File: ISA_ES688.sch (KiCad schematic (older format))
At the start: 108 parts, among them J1 ISA BUS, J2 Interrupt Select, J3 Address Select, J4 DMA Select, J5 Joystick/MIDI, J6 LINE OUT, J7 MIC, J8 LINE IN, J9 SPKR OUT, U1 74LS14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

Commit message: Finished assigning footprints
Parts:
- U3: footprint (none) -> Package_DIP:DIP-16_W7.62mm
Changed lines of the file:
@@
 F 0 "U3" H 8150 15050 60  0000 C CNN
 F 1 "NE558" H 8600 15050 60  0000 C CNN
-F 2 "" H 8900 14500 60  0001 C CNN
+F 2 "Package_DIP:DIP-16_W7.62mm" H 8900 14500 60  0001 C CNN
 F 3 "" H 8900 14500 60  0000 C CNN
 	1    8400 14300

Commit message: Begin laying out parts
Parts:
- removed C3: 100nF, Capacitor_SMD:C_1206_3216Metric_Pad1.33x1.80mm_HandSolder, symbol Device:C_Small
- C10, C13, C14, C15, C16, C17, C18, C19, C25, C5, C6, C7: footprint Capacitor_SMD:C_1206_3216Metric_Pad1.33x1.80mm_HandSolder -> Capacitor_THT:C_Disc_D5.0mm_W2.5mm_P5.00mm
- U2, U4: footprint Package_SO:SOIC-20W_7.5x12.8mm_P1.27mm -> Package_DIP:DIP-20_W7.62mm
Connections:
- net D0: now also U4.2 (A0); no longer U4.9 (A7)
- net D1: now also U4.3 (A1); no longer U4.8 (A6)
- net D2: now also U4.4 (A2); no longer U4.7 (A5)
- net D3: now also U4.5 (A3); no longer U4.6 (A4)
- net D4: now also U4.6 (A4); no longer U4.5 (A3)
- net D5: now also U4.7 (A5); no longer U4.4 (A2)
- net D6: now also U4.8 (A6); no longer U4.3 (A1)
- net D7: now also U4.9 (A7); no longer U4.2 (A0)
- net ES-D0: now also U4.18 (B0); no longer U4.11 (B7)
- net ES-D1: now also U4.17 (B1); no longer U4.12 (B6)
- net ES-D2: now also U4.16 (B2); no longer U4.13 (B5)
- net ES-D3: now also U4.15 (B3); no longer U4.14 (B4)
- net ES-D4: now also U4.14 (B4); no longer U4.15 (B3)
- net ES-D5: now also U4.13 (B5); no longer U4.16 (B2)
- net ES-D6: now also U4.12 (B6); no longer U4.17 (B1)
- net ES-D7: now also U4.11 (B7); no longer U4.18 (B0)
- net GNDA: now also RV1.4; no longer RV1.6
- net at C39.2: now also RV1.6; no longer RV1.4
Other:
- moved on the sheet: U4

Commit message: Begin placing some components on the board
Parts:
- C11, C12: footprint Capacitor_THT:C_Disc_D3.8mm_W2.6mm_P2.50mm -> Capacitor_SMD:C_1206_3216Metric_Pad1.33x1.80mm_HandSolder
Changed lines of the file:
@@
 F 0 "C12" V 10500 7350 50  0000 L CNN
 F 1 "10pF" V 10500 7150 50  0000 L CNN
-F 2 "Capacitor_THT:C_Disc_D3.8mm_W2.6mm_P2.50mm" H 10600 7200 50  0001 C CNN
+F 2 "Capacitor_SMD:C_1206_3216Metric_Pad1.33x1.80mm_HandSolder" H 10600 7200 50  0001 C CNN
 F 3 "~" H 10600 7200 50  0001 C CNN
 	1    10600 7200
@@
 F 0 "C11" V 10500 7150 50  0000 L CNN
 F 1 "10pF" V 10500 6950 50  0000 L CNN
-F 2 "Capacitor_THT:C_Disc_D3.8mm_W2.6mm_P2.50mm" H 10600 7000 50  0001 C CNN
+F 2 "Capacitor_SMD:C_1206_3216Metric_Pad1.33x1.80mm_HandSolder" H 10600 7000 50  0001 C CNN
 F 3 "~" H 10600 7000 50  0001 C CNN
 	1    10600 7000

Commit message: More movement on PCB
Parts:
- J7: footprint Connector_PinHeader_2.54mm:PinHeader_1x02_P2.54mm_Horizontal -> Connector_PinHeader_2.54mm:PinHeader_1x02_P2.54mm_Vertical
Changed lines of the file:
@@
 F 0 "J7" H 15622 3182 50  0000 R CNN
 F 1 "MIC" H 15622 3273 50  0000 R CNN
-F 2 "Connector_PinHeader_2.54mm:PinHeader_1x02_P2.54mm_Horizontal" H 15650 3300 50  0001 C CNN
+F 2 "Connector_PinHeader_2.54mm:PinHeader_1x02_P2.54mm_Vertical" H 15650 3300 50  0001 C CNN
 F 3 "~" H 15650 3300 50  0001 C CNN
 	1    15650 3300

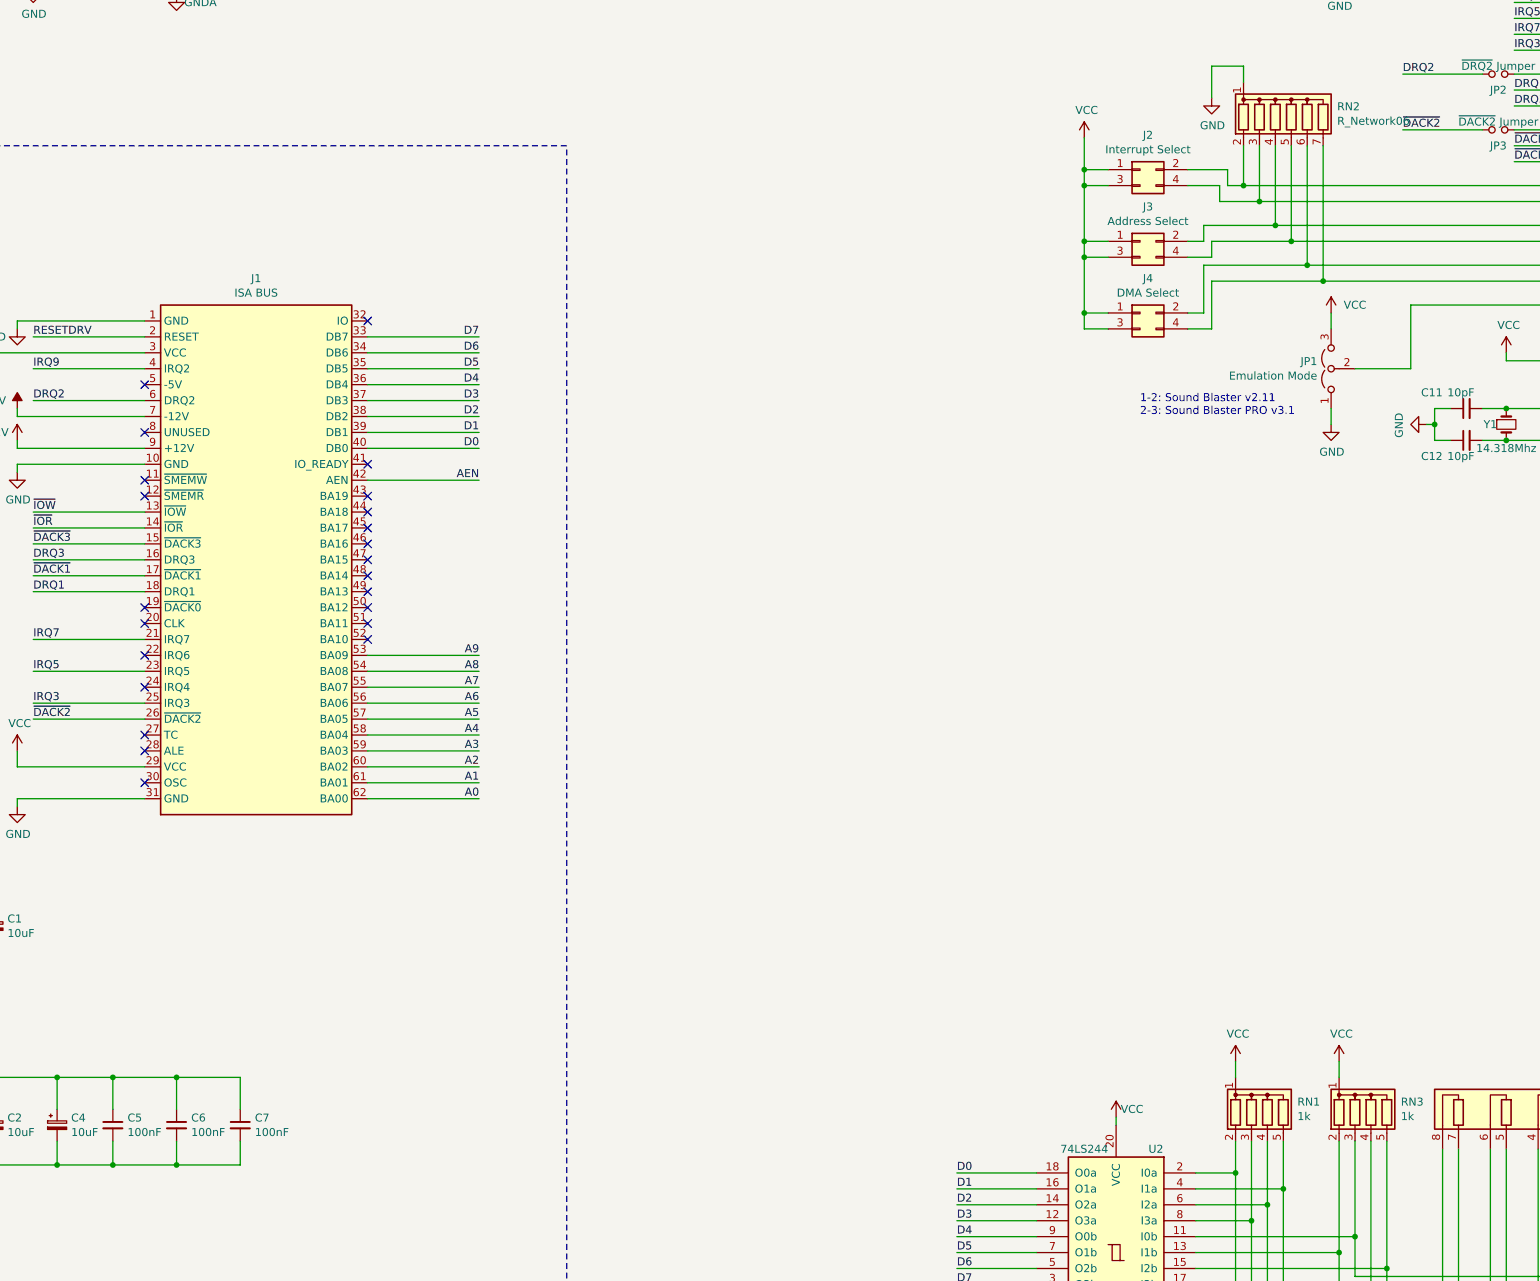
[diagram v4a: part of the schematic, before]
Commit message: Additional trace routing
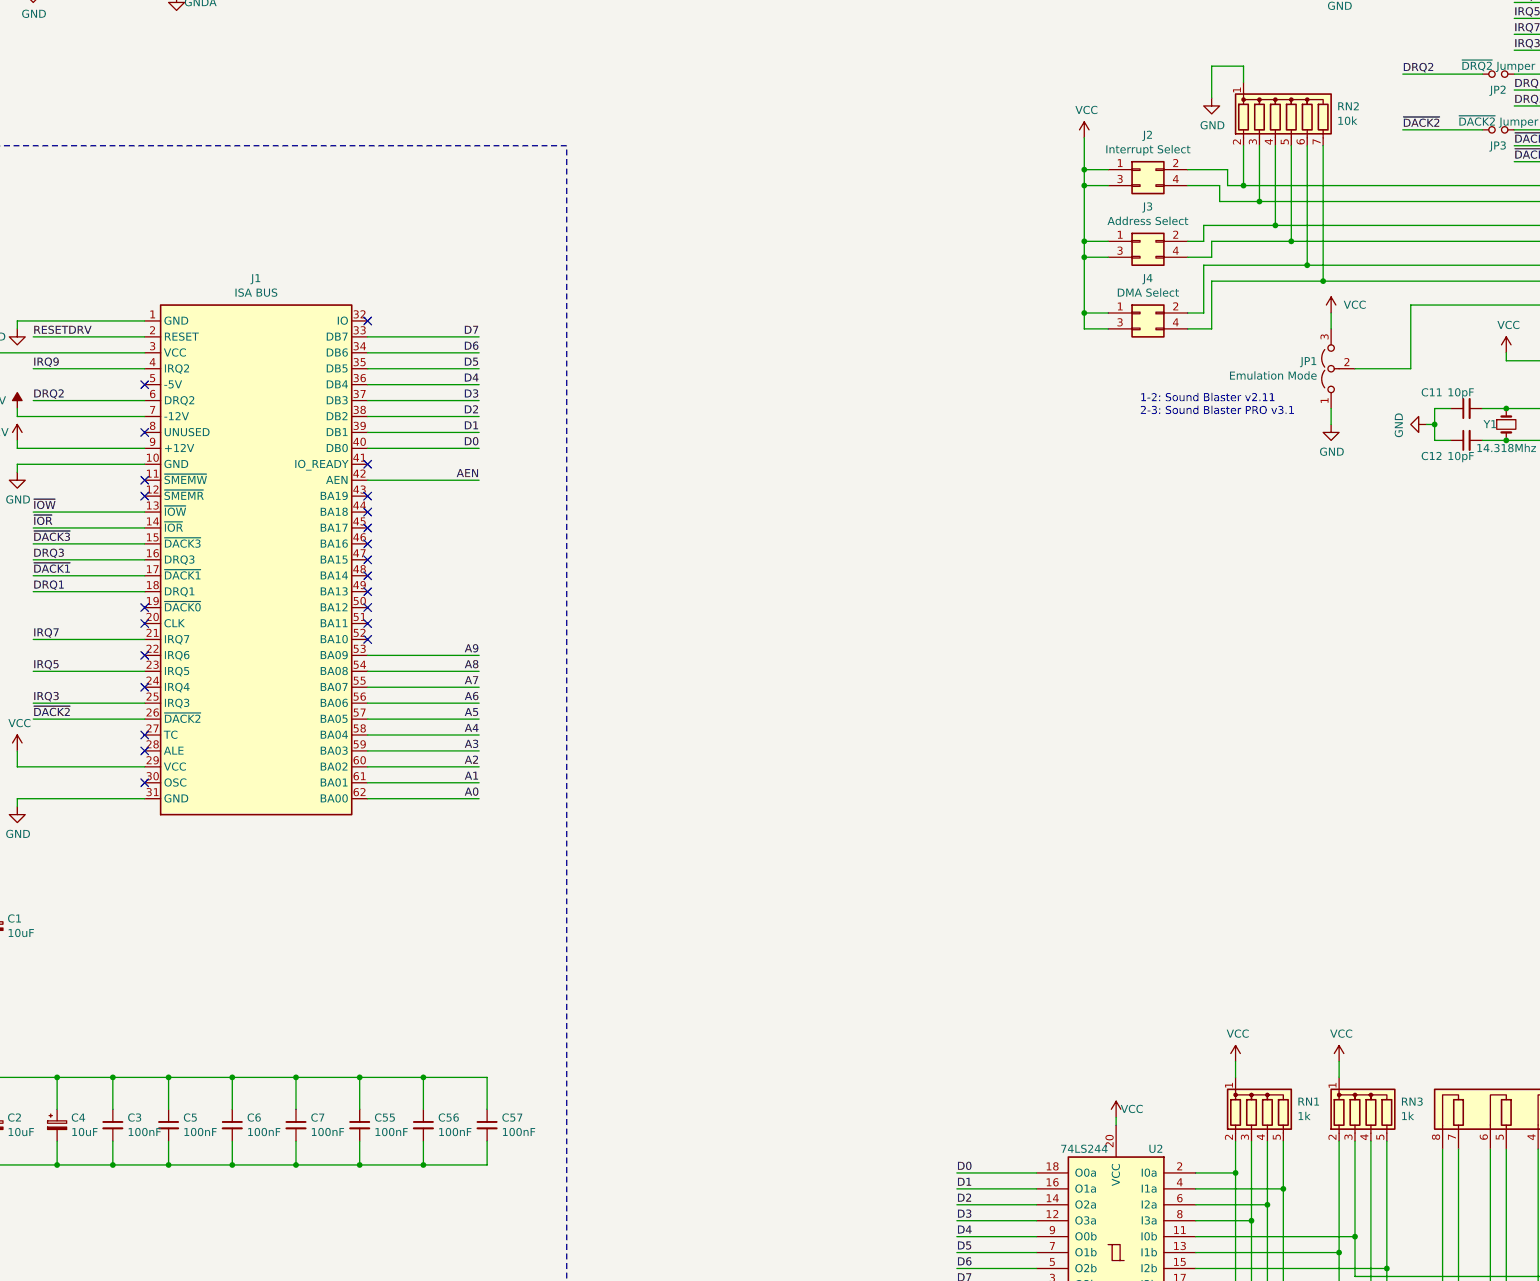
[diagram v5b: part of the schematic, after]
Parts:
- added C3, C55, C56, C57: 100nF, Capacitor_SMD:C_1206_3216Metric_Pad1.33x1.80mm_HandSolder, symbol Device:C_Small
- RN2: value R_Network06 -> 10k
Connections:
- net GND: now also C3.2, C55.2, C56.2, C57.2
- net VCC: now also C3.1, C55.1, C56.1, C57.1
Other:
- moved on the sheet: C5, C6, C7
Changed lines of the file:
@@
 $EndComp
 Wire Wire Line
-	2500 11750 2900 11750
-Connection ~ 2500 11750
-Wire Wire Line
-	2500 11600 2500 11750
-Connection ~ 2100 11750
-Wire Wire Line
-	2900 11750 2900 11600
-Wire Wire Line
-	2100 11750 2500 11750
-Wire Wire Line
-	2500 11200 2900 11200
-Connection ~ 2500 11200
-Wire Wire Line
-	2500 11400 2500 11200
-Connection ~ 2100 11200
-Wire Wire Line
-	2900 11200 2900 11400
-Wire Wire Line
-	2100 11200 2500 11200
+	2850 11750 3250 11750
+Connection ~ 2850 11750
+Wire Wire Line
+	2850 11600 2850 11750
+Connection ~ 2450 11750
+Wire Wire Line
+	3250 11750 3250 11600
+Wire Wire Line
+	2450 11750 2850 11750
+Wire Wire Line
+	2850 11200 3250 11200
+Connection ~ 2850 11200
+Wire Wire Line
+	2850 11400 2850 11200
+Connection ~ 2450 11200
+Wire Wire Line
+	3250 11200 3250 11400
+Wire Wire Line
+	2450 11200 2850 11200
 $Comp
 L Device:C_Small C7
 U 1 1 609B89C1
-P 2900 11500
-F 0 "C7" H 2992 11546 50  0000 L CNN
-F 1 "100nF" H 2992 11455 50  0000 L CNN
-F 2 "Capacitor_THT:C_Disc_D5.0mm_W2.5mm_P5.00mm" H 2900 11500 50  0001 C CNN
-F 3 "~" H 2900 11500 50  0001 C CNN
-	1    2900 11500
+P 3250 11500
+F 0 "C7" H 3342 11546 50  0000 L CNN
+F 1 "100nF" H 3342 11455 50  0000 L CNN
+F 2 "Capacitor_THT:C_Disc_D5.0mm_W2.5mm_P5.00mm" H 3250 11500 50  0001 C CNN
+F 3 "~" H 3250 11500 50  0001 C CNN
+	1    3250 11500
 	1    0    0    -1
 $EndComp
@@
 L Device:C_Small C6
 U 1 1 609B7B2F
-P 2500 11500
-F 0 "C6" H 2592 11546 50  0000 L CNN
-F 1 "100nF" H 2592 11455 50  0000 L CNN
-F 2 "Capacitor_THT:C_Disc_D5.0mm_W2.5mm_P5.00mm" H 2500 11500 50  0001 C CNN
-F 3 "~" H 2500 11500 50  0001 C CNN
-	1    2500 11500
+P 2850 11500
+F 0 "C6" H 2942 11546 50  0000 L CNN
+F 1 "100nF" H 2942 11455 50  0000 L CNN
+F 2 "Capacitor_THT:C_Disc_D5.0mm_W2.5mm_P5.00mm" H 2850 11500 50  0001 C CNN
+F 3 "~" H 2850 11500 50  0001 C CNN
+	1    2850 11500
 	1    0    0    -1
 $EndComp
@@
 NoConn ~ 2300 9050
 Wire Wire Line
-	2100 11600 2100 11750
-Wire Wire Line
-	2100 11400 2100 11200
-Connection ~ 1750 11750
-Wire Wire Line
-	1750 11750 2100 11750
-Connection ~ 1750 11200
-Wire Wire Line
-	1750 11200 2100 11200
+	2450 11600 2450 11750
+Wire Wire Line
+	2450 11400 2450 11200
+Wire Wire Line
+	2100 11750 2450 11750
+Wire Wire Line
+	2100 11200 2450 11200
 $Comp
 L power:VCC #PWR05
@@
 L Device:C_Small C5
 U 1 1 612431D5
-P 2100 11500
-F 0 "C5" H 2192 11546 50  0000 L CNN
-F 1 "100nF" H 2192 11455 50  0000 L CNN
-F 2 "Capacitor_THT:C_Disc_D5.0mm_W2.5mm_P5.00mm" H 2100 11500 50  0001 C CNN
-F 3 "~" H 2100 11500 50  0001 C CNN
-	1    2100 11500
+P 2450 11500
+F 0 "C5" H 2542 11546 50  0000 L CNN
+F 1 "100nF" H 2542 11455 50  0000 L CNN
+F 2 "Capacitor_THT:C_Disc_D5.0mm_W2.5mm_P5.00mm" H 2450 11500 50  0001 C CNN
+F 3 "~" H 2450 11500 50  0001 C CNN
+	1    2450 11500
 	1    0    0    -1
 $EndComp
@@
 P 9500 5150
 F 0 "RN2" H 9788 5196 50  0000 L CNN
-F 1 "R_Network06" H 9788 5105 50  0000 L CNN
+F 1 "10k" H 9788 5105 50  0000 L CNN
 F 2 "Resistor_THT:R_Array_SIP7" V 9875 5150 50  0001 C CNN
 F 3 "http://www.vishay.com/docs/31509/csc.pdf" H 9500 5150 50  0001 C CNN
@@
 Wire Wire Line
 	17300 4700 17300 4750
+Wire Wire Line
+	2100 11600 2100 11750
+Wire Wire Line
+	2100 11400 2100 11200
+Wire Wire Line
+	1750 11750 2100 11750
+Wire Wire Line
+	1750 11200 2100 11200
+$Comp
+L Device:C_Small C3
+U 1 1 61CFC5F5
+P 2100 11500
+F 0 "C3" H 2192 11546 50  0000 L CNN
+F 1 "100nF" H 2192 11455 50  0000 L CNN
+F 2 "Capacitor_SMD:C_1206_3216Metric_Pad1.33x1.80mm_HandSolder" H 2100 11500 50  0001 C CNN
+F 3 "~" H 2100 11500 50  0001 C CNN
+	1    2100 11500
+	1    0    0    -1
+$EndComp
+Connection ~ 1750 11200
+Connection ~ 1750 11750
+Connection ~ 2100 11200
+Connection ~ 2100 11750
+$Comp
+L Device:C_Small C55
+U 1 1 61F8828C
+P 3650 11500
+F 0 "C55" H 3742 11546 50  0000 L CNN
+F 1 "100nF" H 3742 11455 50  0000 L CNN
+F 2 "Capacitor_SMD:C_1206_3216Metric_Pad1.33x1.80mm_HandSolder" H 3650 11500 50  0001 C CNN
+F 3 "~" H 3650 11500 50  0001 C CNN
+	1    3650 11500
+	1    0    0    -1
+$EndComp
+$Comp
+L Device:C_Small C56
+U 1 1 61F8970B
+P 4050 11500
+F 0 "C56" H 4142 11546 50  0000 L CNN
+F 1 "100nF" H 4142 11455 50  0000 L CNN
+F 2 "Capacitor_SMD:C_1206_3216Metric_Pad1.33x1.80mm_HandSolder" H 4050 11500 50  0001 C CNN
+F 3 "~" H 4050 11500 50  0001 C CNN
+	1    4050 11500
+	1    0    0    -1
+$EndComp
+Wire Wire Line
+	3250 11200 3650 11200
+Wire Wire Line
+	4050 11200 4050 11400
+Connection ~ 3250 11200
+Wire Wire Line
+	3650 11400 3650 11200
+Connection ~ 3650 11200
+Wire Wire Line
+	3650 11200 4050 11200
+Wire Wire Line
+	3250 11750 3650 11750
+Wire Wire Line
+	4050 11750 4050 11600
+Connection ~ 3250 11750
+Wire Wire Line
+	3650 11600 3650 11750
+Connection ~ 3650 11750
+Wire Wire Line
+	3650 11750 4050 11750
+$Comp
+L Device:C_Small C57
+U 1 1 621D6566
+P 4450 11500
+F 0 "C57" H 4542 11546 50  0000 L CNN
+F 1 "100nF" H 4542 11455 50  0000 L CNN
+F 2 "Capacitor_SMD:C_1206_3216Metric_Pad1.33x1.80mm_HandSolder" H 4450 11500 50  0001 C CNN
+F 3 "~" H 4450 11500 50  0001 C CNN
+	1    4450 11500
+	1    0    0    -1
+$EndComp
+Wire Wire Line
+	4050 11200 4450 11200
+Wire Wire Line
+	4450 11200 4450 11400
+Connection ~ 4050 11200
+Wire Wire Line
+	4050 11750 4450 11750
+Wire Wire Line
+	4450 11750 4450 11600
+Connection ~ 4050 11750
 $EndSCHEMATC

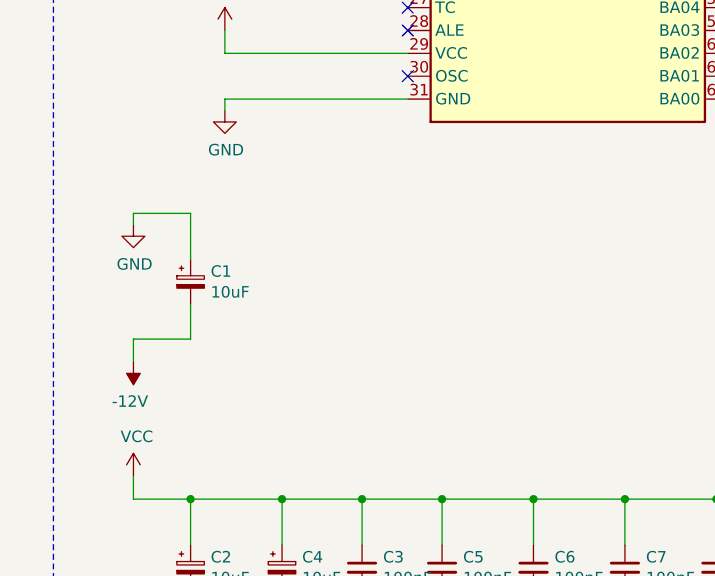
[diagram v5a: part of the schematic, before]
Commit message: Placed all components on PCB
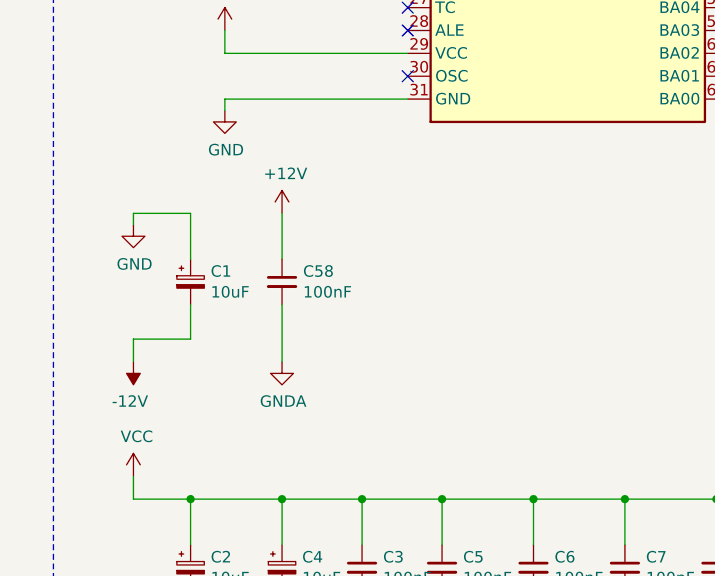
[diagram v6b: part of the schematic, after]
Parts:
- added C58: 100nF, Capacitor_SMD:C_1206_3216Metric_Pad1.33x1.80mm_HandSolder, symbol Device:C_Small
- C8: footprint Capacitor_SMD:C_1206_3216Metric_Pad1.33x1.80mm_HandSolder -> Capacitor_THT:C_Disc_D5.0mm_W2.5mm_P5.00mm
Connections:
- net +12V: now also C58.1
- net GNDA: now also C58.2
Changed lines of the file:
@@
 F 0 "C8" V 7400 13950 50  0000 L CNN
 F 1 "10nF" V 7400 13750 50  0000 L CNN
-F 2 "Capacitor_SMD:C_1206_3216Metric_Pad1.33x1.80mm_HandSolder" H 7500 13800 50  0001 C CNN
+F 2 "Capacitor_THT:C_Disc_D5.0mm_W2.5mm_P5.00mm" H 7500 13800 50  0001 C CNN
 F 3 "~" H 7500 13800 50  0001 C CNN
 	1    7500 13800
@@
 	4450 11750 4450 11600
 Connection ~ 4050 11750
+$Comp
+L Device:C_Small C58
+U 1 1 6232B29C
+P 1750 10250
+F 0 "C58" H 1842 10296 50  0000 L CNN
+F 1 "100nF" H 1842 10205 50  0000 L CNN
+F 2 "Capacitor_SMD:C_1206_3216Metric_Pad1.33x1.80mm_HandSolder" H 1750 10250 50  0001 C CNN
+F 3 "~" H 1750 10250 50  0001 C CNN
+	1    1750 10250
+	1    0    0    -1
+$EndComp
+$Comp
+L power:+12V #PWR0101
+U 1 1 6232F10B
+P 1750 9950
+F 0 "#PWR0101" H 1750 9800 50  0001 C CNN
+F 1 "+12V" H 1765 10123 50  0000 C CNN
+F 2 "" H 1750 9950 50  0001 C CNN
+F 3 "" H 1750 9950 50  0001 C CNN
+	1    1750 9950
+	1    0    0    -1
+$EndComp
+Wire Wire Line
+	1750 9950 1750 10150
+$Comp
+L power:GNDA #PWR0102
+U 1 1 6245A246
+P 1750 10600
+F 0 "#PWR0102" H 1750 10350 50  0001 C CNN
+F 1 "GNDA" H 1755 10427 50  0000 C CNN
+F 2 "" H 1750 10600 50  0001 C CNN
+F 3 "" H 1750 10600 50  0001 C CNN
+	1    1750 10600
+	1    0    0    -1
+$EndComp
+Wire Wire Line
+	1750 10350 1750 10600
 $EndSCHEMATC
